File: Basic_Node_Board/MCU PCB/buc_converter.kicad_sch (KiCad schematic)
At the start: 13 parts, among them J2 Conn_01x02, U1 TPS54560BQDDARQ1

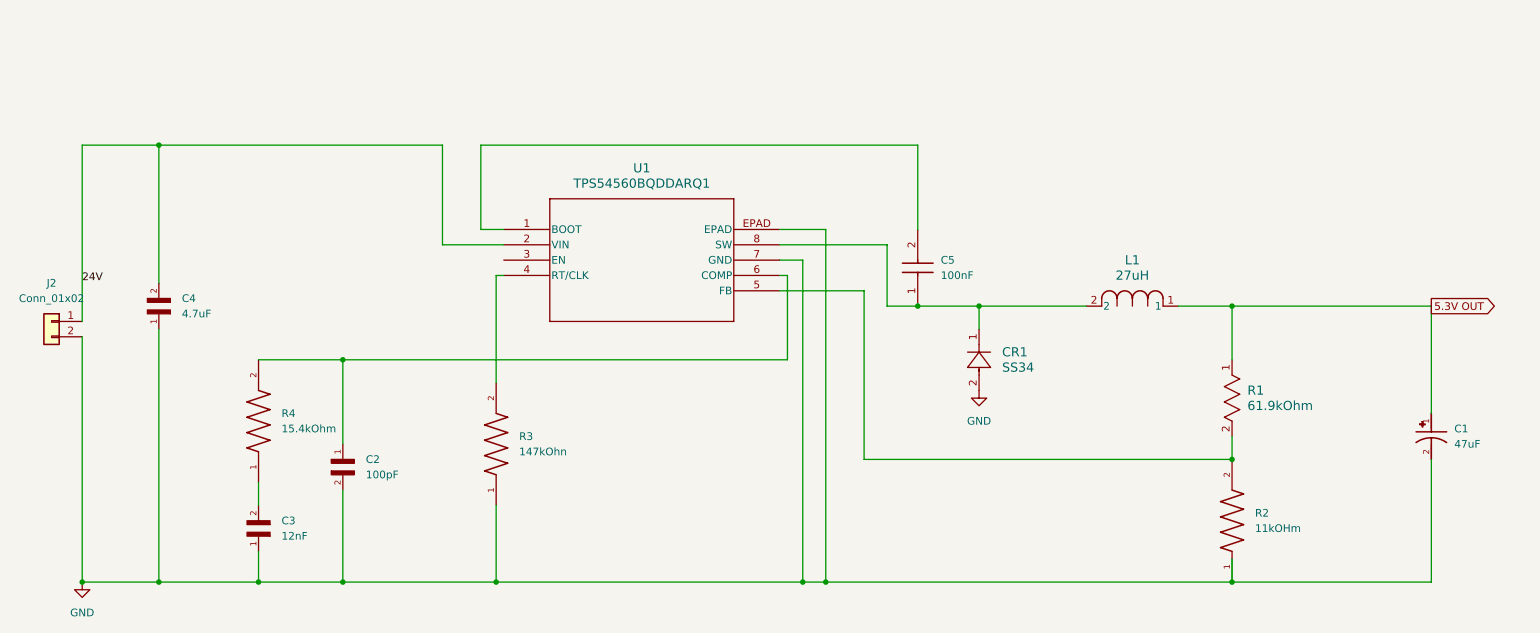
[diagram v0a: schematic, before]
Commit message: fixed the buck converter
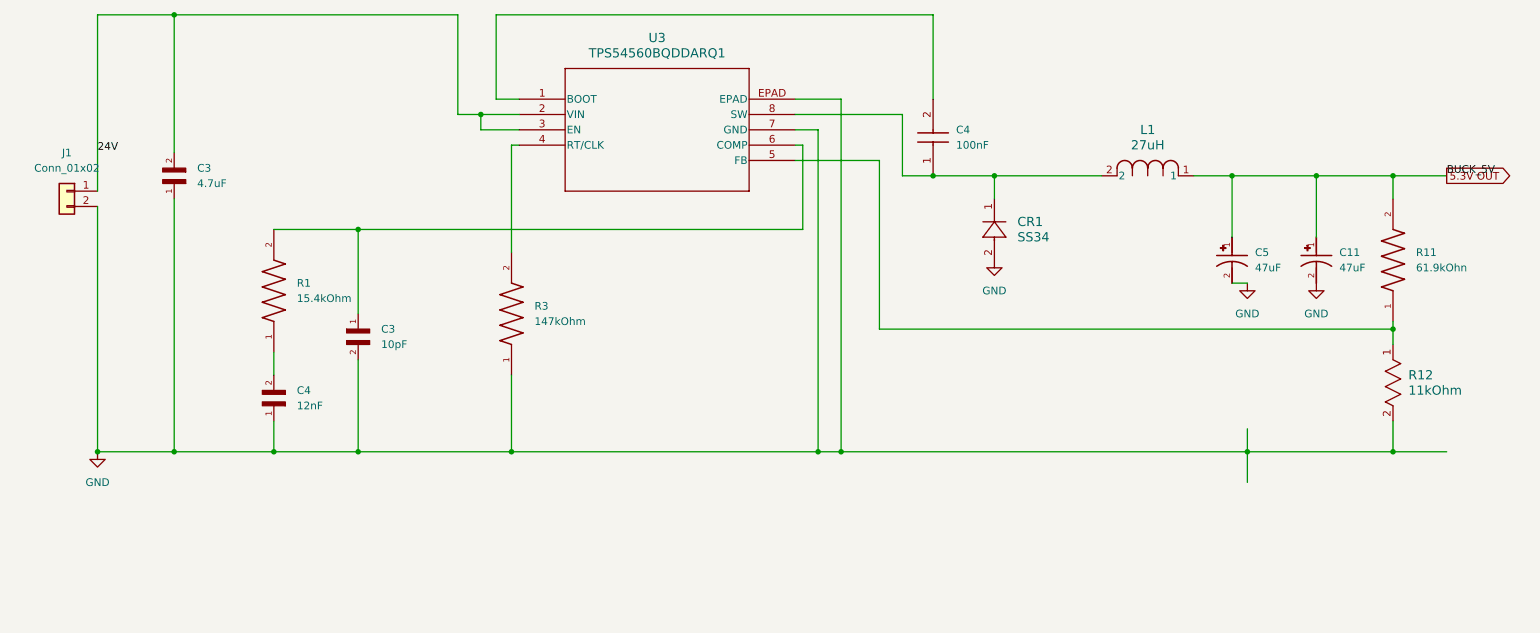
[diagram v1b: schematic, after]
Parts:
- removed C1: 47uF, Capacitor_SMD:C_0402_1005Metric_Pad0.74x0.62mm_HandSolder, symbol 10TPE47MAZB:10TPE47MAZB
- removed C2: 100pF, Capacitor_SMD:C_0603_1608Metric_Pad1.08x0.95mm_HandSolder, symbol CL05C110JB5NNNC:CL05C110JB5NNNC
- removed C5: 100nF, Capacitor_SMD:C_0504_1310Metric_Pad0.83x1.28mm_HandSolder, symbol 08053C104KAT2A:08053C104KAT2A
- removed J2: Conn_01x02, Connector_PinHeader_2.54mm:PinHeader_1x04_P2.54mm_Vertical, symbol Connector_Generic:Conn_01x02
- removed R1: 61.9kOhm, Resistor_SMD:R_0201_0603Metric_Pad0.64x0.40mm_HandSolder, symbol 2026-02-07_22-08-15:CRCW040261K9FKED
- removed R2: 11kOHm, Resistor_SMD:R_0201_0603Metric_Pad0.64x0.40mm_HandSolder, symbol CRCW040211K0FKED:CRCW040211K0FKED
- removed R4: 15.4kOhm, Resistor_SMD:R_0201_0603Metric_Pad0.64x0.40mm_HandSolder, symbol RC0201FR-0723K7L:RC0201FR-0723K7L
- removed U1: TPS54560BQDDARQ1, PROVE-footprints:VREG_LM5017MR_NOPB, symbol TPS54560BQDDARQ1:TPS54560BQDDARQ1
- added C11, C5: 47uF, Capacitor_SMD:C_1206_3216Metric_Pad1.33x1.80mm_HandSolder, symbol 10TPE47MAZB:10TPE47MAZB
- added C3: 10pF, Capacitor_SMD:C_1206_3216Metric_Pad1.33x1.80mm_HandSolder, symbol CL05C110JB5NNNC:CL05C110JB5NNNC
- added C4: 100nF, Capacitor_SMD:C_1206_3216Metric_Pad1.33x1.80mm_HandSolder, symbol 08053C104KAT2A:08053C104KAT2A
- added J1: Conn_01x02, Connector_PinHeader_1.00mm:PinHeader_1x02_P1.00mm_Vertical, symbol Connector_Generic:Conn_01x02
- added R1: 15.4kOhm, Resistor_SMD:R_1206_3216Metric_Pad1.30x1.75mm_HandSolder, symbol RC0201FR-0723K7L:RC0201FR-0723K7L
- added R11: 61.9kOhn, Resistor_SMD:R_1206_3216Metric_Pad1.30x1.75mm_HandSolder, symbol CRCW040211K0FKED:CRCW040211K0FKED
- added R12: 11kOhm, Resistor_SMD:R_1206_3216Metric_Pad1.30x1.75mm_HandSolder, symbol 2026-02-07_22-08-15:CRCW040261K9FKED
- added U3: TPS54560BQDDARQ1, PROVE-footprints:VREG_LM5017MR_NOPB, symbol TPS54560BQDDARQ1:TPS54560BQDDARQ1
- C3: renamed from C4; footprint Capacitor_SMD:C_0504_1310Metric_Pad0.83x1.28mm_HandSolder -> Capacitor_SMD:C_1206_3216Metric_Pad1.33x1.80mm_HandSolder
- C4: renamed from C3; footprint Capacitor_SMD:C_0504_1310Metric_Pad0.83x1.28mm_HandSolder -> Capacitor_SMD:C_1206_3216Metric_Pad1.33x1.80mm_HandSolder
- CR1: footprint Diode_SMD:D_0201_0603Metric_Pad0.64x0.40mm_HandSolder -> Diode_SMD:D_1206_3216Metric_Pad1.42x1.75mm_HandSolder
- L1: footprint Inductor_SMD:L_0201_0603Metric_Pad0.64x0.40mm_HandSolder -> Inductor_SMD:L_1206_3216Metric_Pad1.22x1.90mm_HandSolder
- R3: value 147kOhn -> 147kOhm; footprint Resistor_SMD:R_0201_0603Metric_Pad0.64x0.40mm_HandSolder -> Resistor_SMD:R_1206_3216Metric_Pad1.30x1.75mm_HandSolder
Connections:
- net 24V: now also J1.1 (Pin_1), U3.2 (VIN), U3.3 (EN)
- net 5.3V OUT: now also C11.1, C5.1, R11.2
- net GND: now also C11.2, C3.2, C5.2, J1.2 (Pin_2), R12.2, U3.7 (GND), U3.EPAD
- net at R3.2: now also U3.4 (RT/CLK)
- net at CR1.1, L1.2: now also C4.1, U3.8 (SW)
- net at C4.2: now also R1.1
- new net: R11.1, R12.1, U3.5 (FB)
- new net: C3.1, R1.2, U3.6 (COMP)
- new net: C4.2, U3.1 (BOOT)
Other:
- company: PROVE Lab - Low Voltage -> (none)
- title: 24V_to_5.3_Buck_Converter -> (none)
- moved on the sheet: C3, C4, CR1, L1
